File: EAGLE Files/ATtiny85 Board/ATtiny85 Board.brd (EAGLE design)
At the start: 20.3 x 18.7 mm, 10 parts

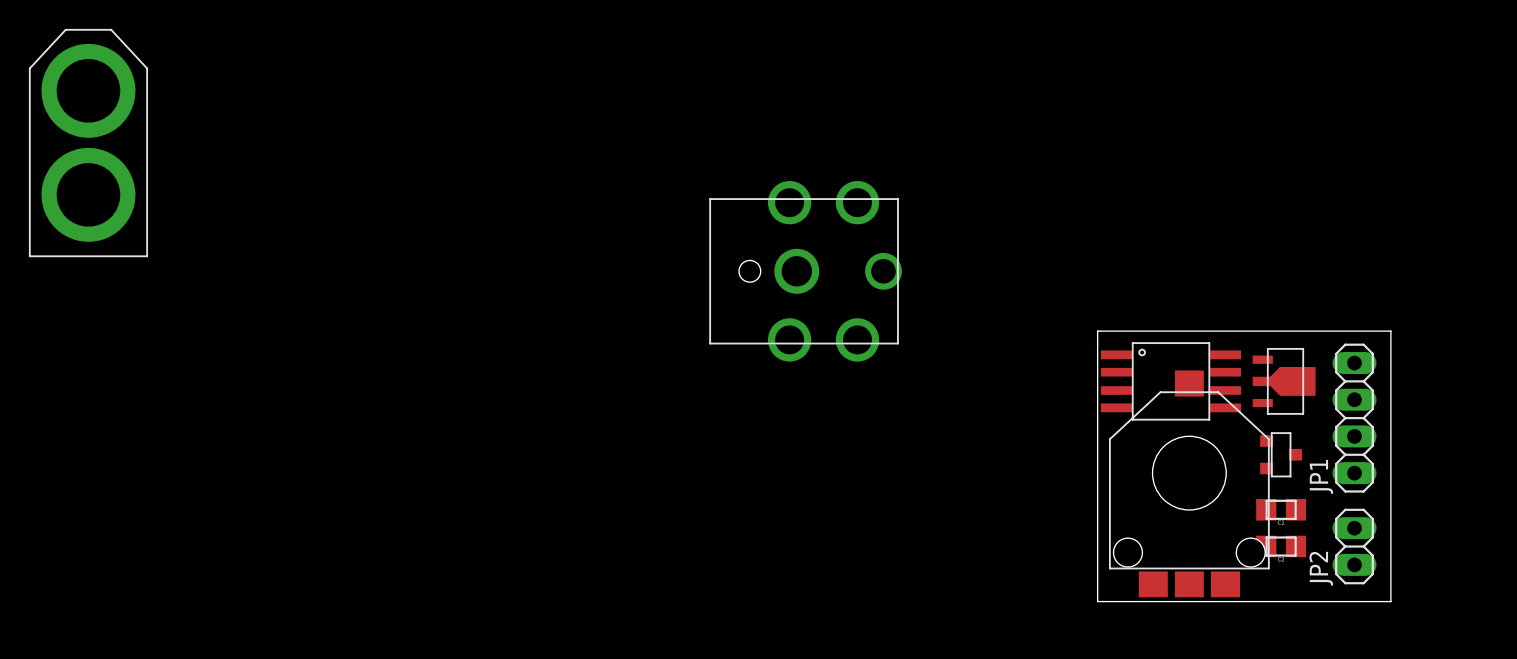
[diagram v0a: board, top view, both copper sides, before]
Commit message: Enlarged and repositioned vias for easier milling and soldering
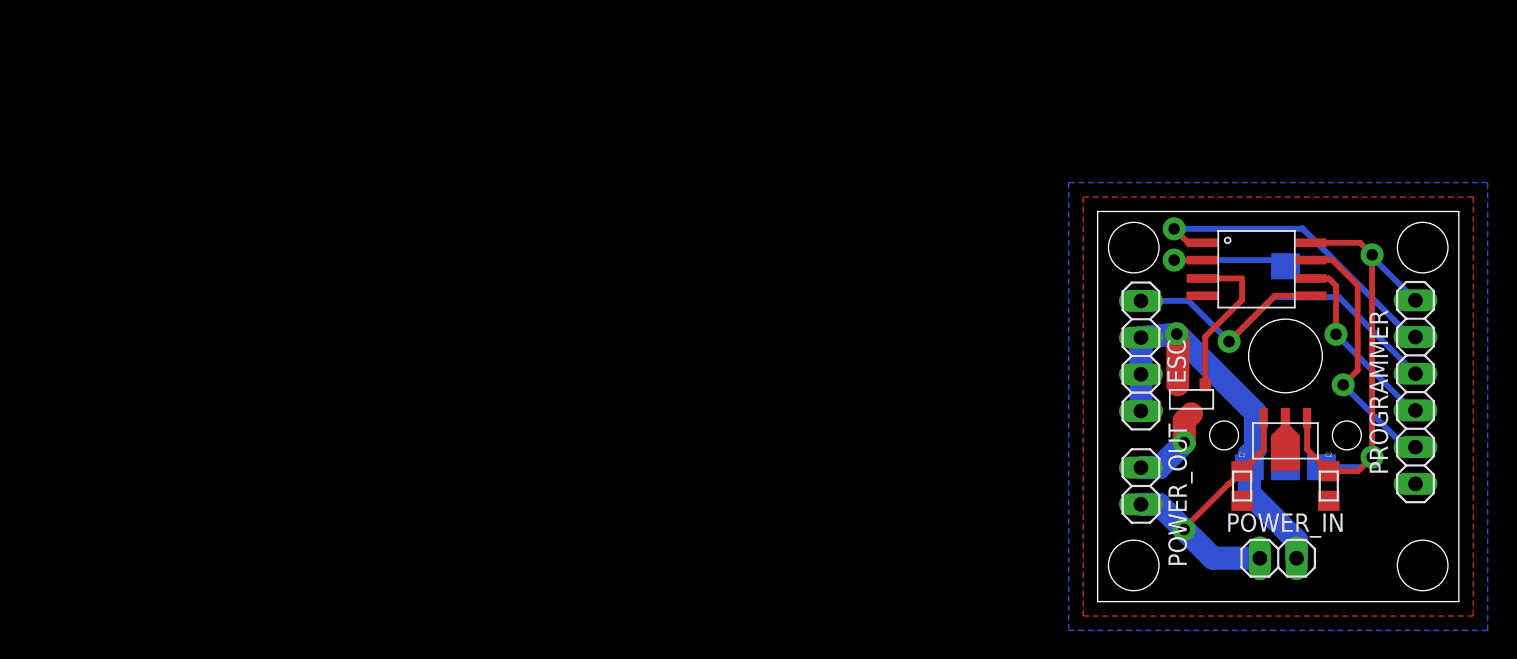
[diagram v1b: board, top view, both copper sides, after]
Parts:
- removed BARREL: PJ-082BH, Controls Library:PJ-082BH
- removed JP1: (no value), Controls Library:1X04
- removed JP2: M02, Controls Library:1X02
- removed U$2: XT60, Controls Library:XT60
- added ESC: (no value), Controls Library:1X04
- added POWER_IN, POWER_OUT: (no value), Controls Library:1X02
- added PROGRAMMER: (no value), Controls Library:1X06
- moved SENSOR 10.5 mm to (13.0, 17.0), flipped to the bottom
- moved U$1 9.76 mm to (11.0, 23.0)
- moved MOSFET 7.29 mm to (6.50, 14.0), turned to 180 degrees
- moved C2 5.33 mm to (16.0, 8.00), turned to 270 degrees
- moved C1 3.16 mm to (10.0, 8.00), turned to 270 degrees
- moved REG 2.99 mm to (13.0, 12.7), turned to 180 degrees
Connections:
- net 12V_SUPPLY: now also POWER_IN.1, POWER_OUT.1; no longer BARREL.1, U$2.+
- net 5V_SUPPLY: now also PROGRAMMER.1
- net GND: now also ESC.2, ESC.3, ESC.4, POWER_IN.2, PROGRAMMER.6; no longer BARREL.2, BARREL.SH1, BARREL.SH2, BARREL.SH3, BARREL.SH4, JP2.2
- net MISO: now also PROGRAMMER.4; no longer JP1.3
- net MOSI/ESC: now also ESC.1, PROGRAMMER.3; no longer JP1.2, JP2.1
- net N$3: now also POWER_OUT.2; no longer U$2.-
- net RESET: now also PROGRAMMER.2; no longer JP1.1
- net SCK: now also PROGRAMMER.5; no longer JP1.4
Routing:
- net 5V_SUPPLY: track 0.00 -> 34.5 mm, vias 0 -> 2
- net MOSI/ESC: track 0.00 -> 30.8 mm, vias 0 -> 1
- net GND: track 0.00 -> 30.4 mm, vias 0 -> 1
- net RESET: track 0.00 -> 22.2 mm, vias 0 -> 1
- net 12V_SUPPLY: track 0.00 -> 19.8 mm, vias 0 -> 1
- net SCK: track 0.00 -> 18.1 mm, vias 0 -> 1
- net MISO: track 0.00 -> 13.0 mm, vias 0 -> 1
- net DRIVE: track 0.00 -> 11.2 mm
- net SENSE: track 0.00 -> 10.6 mm, vias 0 -> 1
- net N$3: track 0.00 -> 5.92 mm, vias 0 -> 1
- added copper zone on layer 1, net GND
- added copper zone on layer 16, net GND
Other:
- board size 20.3 x 18.7 mm -> 25 x 27 mm
